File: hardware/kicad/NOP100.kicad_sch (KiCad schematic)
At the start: 44 parts, among them CON1 MIKROBUS_MODULE_CONN, CON2 MIKROBUS_MODULE_CONN, J1 CAN, Q1 BSS138, Q2 BSS138, SW1 BUS, SW2 SW_Push, U1 NCS1S1205SC, U2 MCP2551-I-P, U3 Teensy_4.0, U4 74HC165, U6 NCS1S1203SC

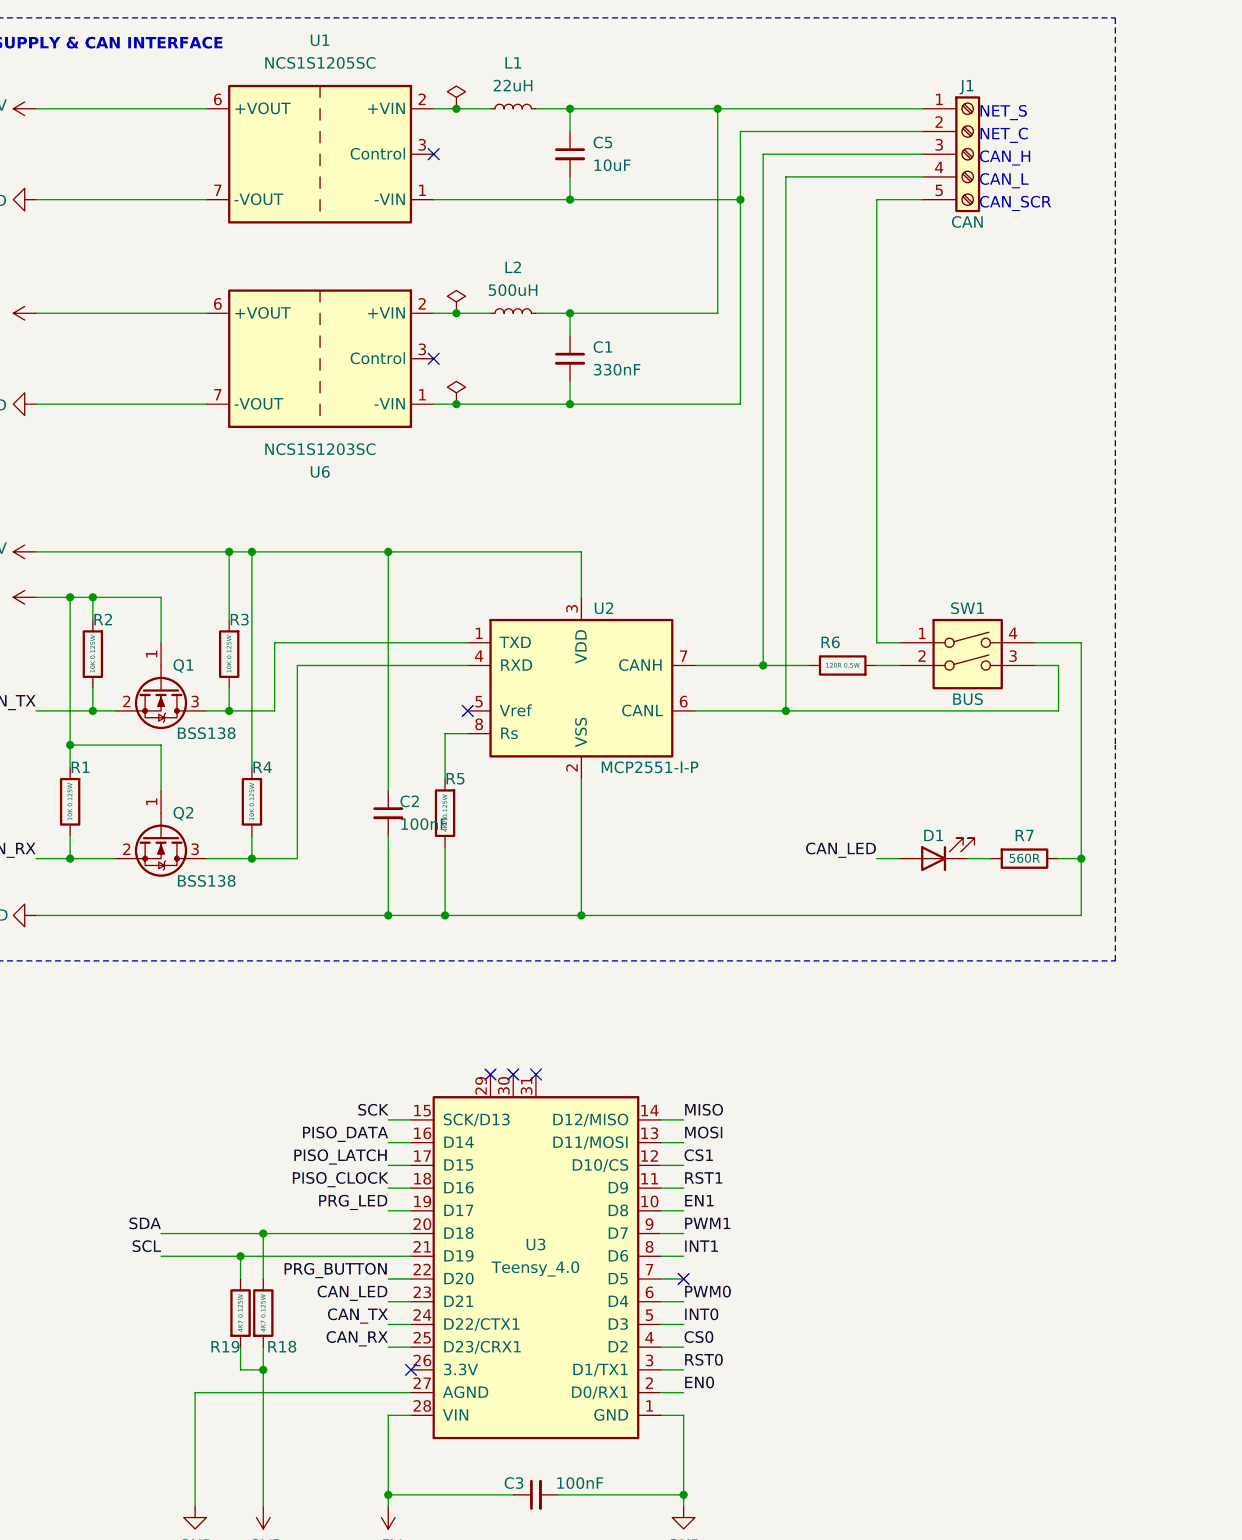
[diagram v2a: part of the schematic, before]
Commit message: Add 3.3VDC alternatives.
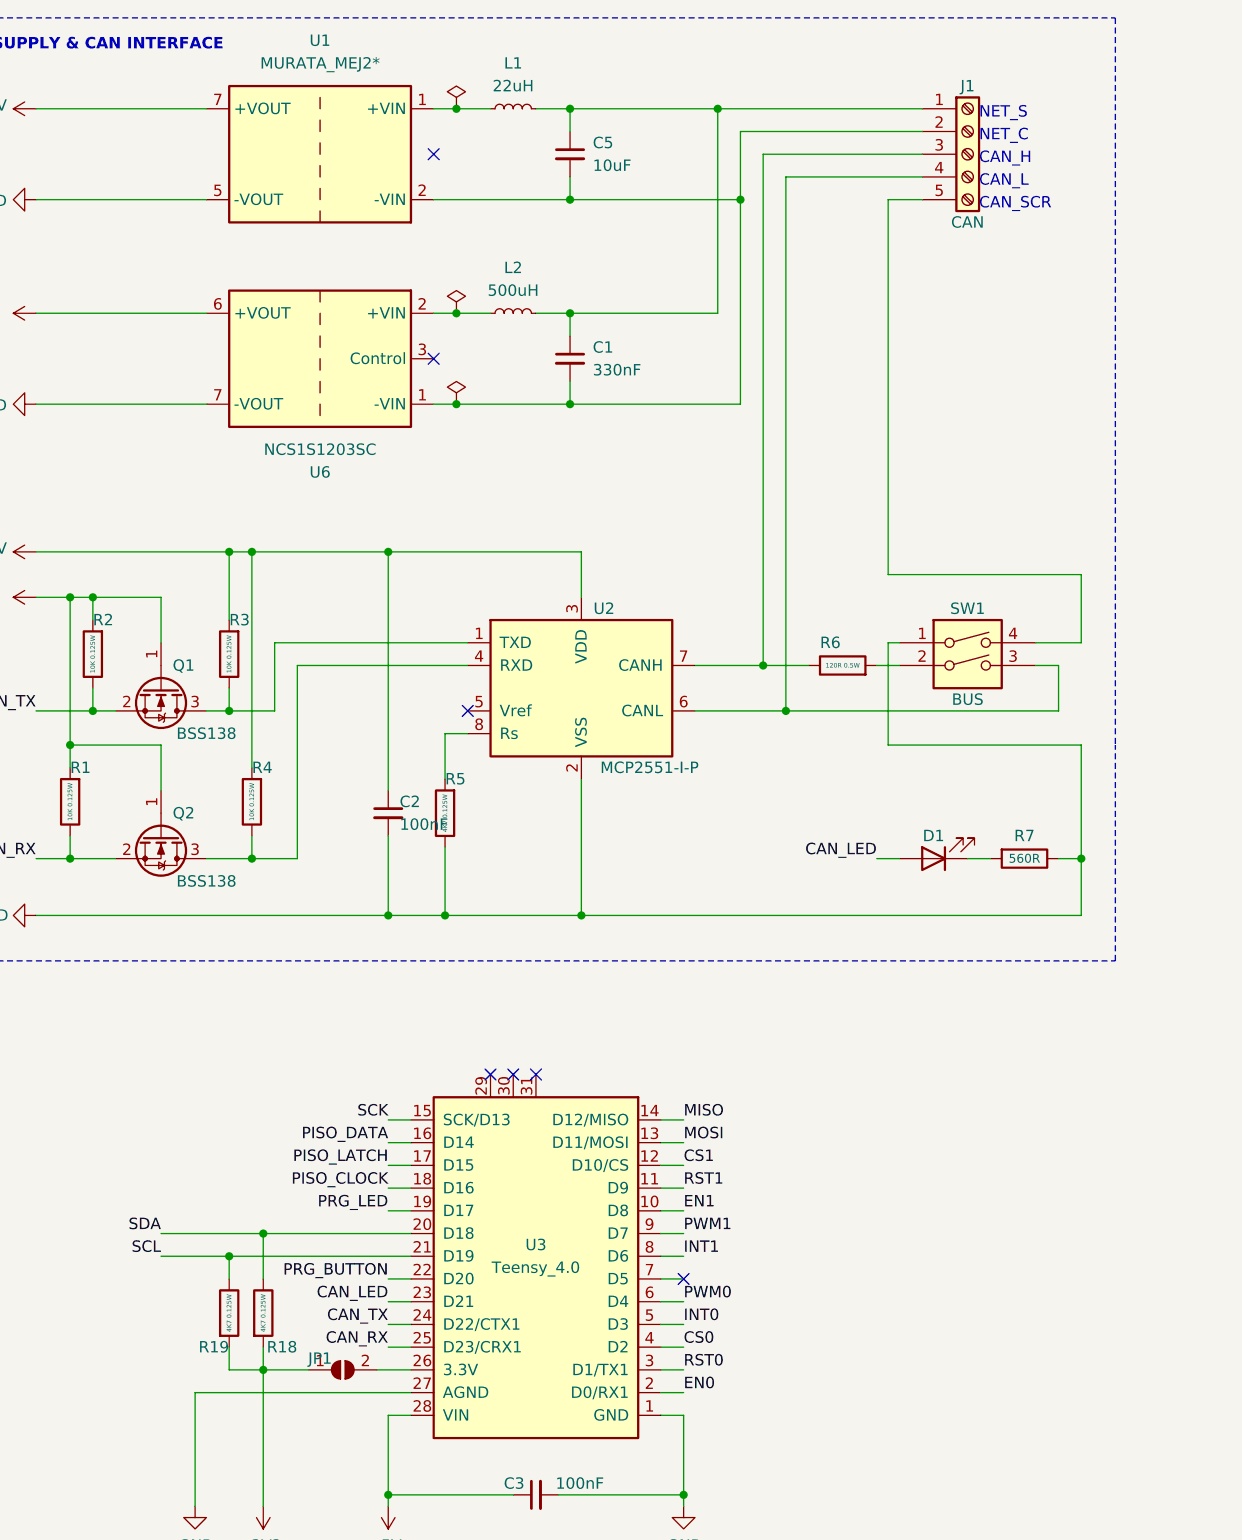
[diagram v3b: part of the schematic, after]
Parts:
- removed U1: NCS1S1205SC, Converter_DCDC:Converter_DCDC_Murata_NCS1SxxxxSC_THT, symbol Converter_DCDC:NCS1S1205SC
- added JP1: SolderJumper_2_Open, Jumper:SolderJumper-2_P1.3mm_Bridged_RoundedPad1.0x1.5mm, symbol Jumper:SolderJumper_2_Open
- added U1: MURATA_MEJ2*, pdjr:Murata-MEJ2*, symbol pdjr:MURATA_MEJ2*
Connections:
- net +3V3: now also JP1.1 (A)
- net +5V: now also U1.7 (+VOUT)
- net GND: now also SW1.1, U1.5 (-VOUT); no longer SW1.4
- net at J1.5 (Pin_5): now also SW1.4; no longer SW1.1
- net at C1.2, C5.2, J1.2 (Pin_2)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: now also U1.2 (-VIN)
- net at L1.1: now also U1.1 (+VIN)
- net at U3.26 (3.3V): now also JP1.2 (B)
- no-connect marks 15 -> 14
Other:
- moved on the sheet: R19
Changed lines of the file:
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@@
   (junction (at 199.39 71.12) (diameter 0) (color 0 0 0 0)
   )
+  (junction (at 144.78 107.95) (diameter 0) (color 0 0 0 0)
+  )
   (junction (at 53.34 165.1) (diameter 0) (color 0 0 0 0)
   )
@@
   (junction (at 240.03 41.91) (diameter 0) (color 0 0 0 0)
   )
-  (junction (at 144.78 107.95) (diameter 0) (color 0 0 0 0)
-  )
   (junction (at 237.49 39.37) (diameter 0) (color 0 0 0 0)
   )
@@
   (junction (at 88.9 114.3) (diameter 0) (color 0 0 0 0)
   )
-  (junction (at 50.8 152.4) (diameter 0) (color 0 0 0 0)
+  (junction (at 49.53 152.4) (diameter 0) (color 0 0 0 0)
   )
   (junction (at 194.31 71.12) (diameter 0) (color 0 0 0 0)
@@
   (junction (at 106.68 34.29) (diameter 0) (color 0 0 0 0)
   )
-  (no_connect (at 69.85 165.1))
   (no_connect (at 201.93 34.29))
   (no_connect (at 72.39 29.21))
@@
     (stroke (width 0) (type default))
   )
-  (wire (pts (xy 50.8 152.4) (xy 50.8 154.94))
+  (wire (pts (xy 49.53 152.4) (xy 49.53 154.94))
     (stroke (width 0) (type default))
   )
@@
     (stroke (width 0) (type default))
   )
-  (wire (pts (xy 50.8 165.1) (xy 50.8 162.56))
+  (wire (pts (xy 49.53 165.1) (xy 49.53 162.56))
     (stroke (width 0) (type default))
   )
@@
     (stroke (width 0) (type default))
   )
+  (wire (pts (xy 144.78 83.82) (xy 144.78 76.2))
+    (stroke (width 0) (type default))
+  )
   (wire (pts (xy 205.74 97.79) (xy 213.36 97.79))
     (stroke (width 0) (type default))
@@
     (stroke (width 0) (type default))
   )
-  (wire (pts (xy 121.92 34.29) (xy 121.92 83.82))
+  (wire (pts (xy 123.19 34.29) (xy 123.19 76.2))
     (stroke (width 0) (type default))
   )
@@
     (stroke (width 0) (type default))
   )
+  (wire (pts (xy 49.53 152.4) (xy 69.85 152.4))
+    (stroke (width 0) (type default))
+  )
   (wire (pts (xy 87.63 57.15) (xy 106.68 57.15))
     (stroke (width 0) (type default))
@@
     (stroke (width 0) (type default))
   )
-  (wire (pts (xy 144.78 83.82) (xy 144.78 107.95))
+  (wire (pts (xy 124.46 83.82) (xy 123.19 83.82))
     (stroke (width 0) (type default))
   )
@@
     (stroke (width 0) (type default))
   )
-  (wire (pts (xy 53.34 165.1) (xy 50.8 165.1))
-    (stroke (width 0) (type default))
-  )
-  (wire (pts (xy 121.92 34.29) (xy 127 34.29))
+  (wire (pts (xy 53.34 165.1) (xy 49.53 165.1))
+    (stroke (width 0) (type default))
+  )
+  (wire (pts (xy 123.19 34.29) (xy 127 34.29))
     (stroke (width 0) (type default))
   )
@@
     (stroke (width 0) (type dash))
   )
+  (wire (pts (xy 144.78 95.25) (xy 144.78 107.95))
+    (stroke (width 0) (type default))
+  )
   (wire (pts (xy 227.33 59.69) (xy 224.79 59.69))
     (stroke (width 0) (type default))
@@
     (stroke (width 0) (type default))
   )
+  (wire (pts (xy 123.19 95.25) (xy 144.78 95.25))
+    (stroke (width 0) (type default))
+  )
   (wire (pts (xy 67.31 139.7) (xy 69.85 139.7))
     (stroke (width 0) (type default))
@@
   )
   (wire (pts (xy 72.39 24.13) (xy 74.93 24.13))
-    (stroke (width 0) (type default))
-  )
-  (wire (pts (xy 50.8 152.4) (xy 69.85 152.4))
     (stroke (width 0) (type default))
   )
@@
     (stroke (width 0) (type default))
   )
+  (wire (pts (xy 53.34 165.1) (xy 58.42 165.1))
+    (stroke (width 0) (type default))
+  )
   (wire (pts (xy 142.24 91.44) (xy 142.24 86.36))
     (stroke (width 0) (type default))
@@
   )
   (wire (pts (xy 104.14 24.13) (xy 127 24.13))
+    (stroke (width 0) (type default))
+  )
+  (wire (pts (xy 123.19 83.82) (xy 123.19 95.25))
     (stroke (width 0) (type default))
   )
@@
     (stroke (width 0) (type default))
   )
+  (wire (pts (xy 123.19 76.2) (xy 144.78 76.2))
+    (stroke (width 0) (type default))
+  )
   (wire (pts (xy 97.79 137.16) (xy 100.33 137.16))
     (stroke (width 0) (type default))
@@
     (stroke (width 0) (type default))
   )
-  (wire (pts (xy 121.92 83.82) (xy 124.46 83.82))
-    (stroke (width 0) (type default))
-  )
   (wire (pts (xy 73.66 106.68) (xy 73.66 114.3))
     (stroke (width 0) (type default))
@@
     (stroke (width 0) (type default))
   )
-  (wire (pts (xy 41.91 152.4) (xy 50.8 152.4))
+  (wire (pts (xy 41.91 152.4) (xy 49.53 152.4))
     (stroke (width 0) (type default))
   )
@@
   )
   (wire (pts (xy 109.22 86.36) (xy 114.3 86.36))
+    (stroke (width 0) (type default))
+  )
+  (wire (pts (xy 66.04 165.1) (xy 69.85 165.1))
     (stroke (width 0) (type default))
   )
@@
     )
   )
+  (symbol (lib_id "pdjr:MURATA_MEJ2*") (at 59.69 29.21 180) (unit 1)
+    (in_bom yes) (on_board yes) (dnp no) (fields_autoplaced)
+    (property "Reference" "U1" (at 59.69 16.51 0)
+      (effects (font (size 1.27 1.27)))
+    )
+    (property "Value" "MURATA_MEJ2*" (at 59.69 19.05 0)
+      (effects (font (size 1.27 1.27)))
+    )
+    (property "Footprint" "pdjr:Murata-MEJ2*" (at 59.69 19.05 0)
+      (effects (font (size 1.27 1.27)) hide)
+    )
+    (property "Datasheet" "https://power.murata.com/data/power/ncl/kdc_ncs1.pdf" (at 60.325 29.21 0)
+      (effects (font (size 1.27 1.27)) hide)
+    )
+    (pin "2")
+    (pin "7")
+    (pin "5")
+    (pin "1")
+    (instances
+      (project "NOP100"
+        (path "/2cdb9afa-f75f-4c95-9ee5-dd44c25e8877"
+          (reference "U1") (unit 1)
+        )
+      )
+    )
+  )
   (symbol (lib_id "power:PWR_FLAG") (at 74.93 57.15 0) (unit 1)
     (in_bom yes) (on_board yes) (dnp no) (fields_autoplaced)
@@
     )
   )
-  (symbol (lib_id "Device:R") (at 50.8 158.75 0) (unit 1)
-    (in_bom yes) (on_board yes) (dnp no)
-    (property "Reference" "R19" (at 50.8 162.56 0)
+  (symbol (lib_id "Device:R") (at 49.53 158.75 0) (unit 1)
+    (in_bom yes) (on_board yes) (dnp no)
+    (property "Reference" "R19" (at 49.53 162.56 0)
       (effects (font (size 1.27 1.27)) (justify right))
     )
-    (property "Value" "4K7 0.125W" (at 50.8 158.75 90)
+    (property "Value" "4K7 0.125W" (at 49.53 158.75 90)
       (effects (font (size 0.508 0.508)))
     )
-    (property "Footprint" "Resistor_SMD:R_0805_2012Metric" (at 49.022 158.75 90)
-      (effects (font (size 1.27 1.27)) hide)
-    )
-    (property "Datasheet" "~" (at 50.8 158.75 0)
+    (property "Footprint" "Resistor_SMD:R_0805_2012Metric" (at 47.752 158.75 90)
+      (effects (font (size 1.27 1.27)) hide)
+    )
+    (property "Datasheet" "~" (at 49.53 158.75 0)
       (effects (font (size 1.27 1.27)) hide)
     )
@@
     )
   )
+  (symbol (lib_id "Jumper:SolderJumper_2_Open") (at 62.23 165.1 0) (unit 1)
+    (in_bom yes) (on_board yes) (dnp no)
+    (property "Reference" "JP1" (at 59.69 163.83 0)
+      (effects (font (size 1.27 1.27)))
+    )
+    (property "Value" "SolderJumper_2_Open" (at 62.23 161.29 0)
+      (effects (font (size 1.27 1.27)) hide)
+    )
+    (property "Footprint" "Jumper:SolderJumper-2_P1.3mm_Bridged_RoundedPad1.0x1.5mm" (at 62.23 165.1 0)
+      (effects (font (size 1.27 1.27)) hide)
+    )
+    (property "Datasheet" "~" (at 62.23 165.1 0)
+      (effects (font (size 1.27 1.27)) hide)
+    )
+    (pin "2")
+    (pin "1")
+    (instances
+      (project "NOP100"
+        (path "/2cdb9afa-f75f-4c95-9ee5-dd44c25e8877"
+          (reference "JP1") (unit 1)
+        )
+      )
+    )
+  )
   (symbol (lib_id "Device:C_Small") (at 87.63 29.21 0) (unit 1)
     (in_bom yes) (on_board yes) (dnp no) (fields_autoplaced)
@@
         )
       )
-    )
-  )
-  (symbol (lib_id "Converter_DCDC:NCS1S1205SC") (at 59.69 29.21 0) (mirror y) (unit 1)
-    (in_bom yes) (on_board yes) (dnp no)
-    (property "Reference" "U1" (at 59.69 16.51 0)
-      (effects (font (size 1.27 1.27)))
-    )
-    (property "Value" "NCS1S1205SC" (at 59.69 19.05 0)
-      (effects (font (size 1.27 1.27)))
-    )
-    (property "Footprint" "Converter_DCDC:Converter_DCDC_Murata_NCS1SxxxxSC_THT" (at 59.69 39.37 0)
-      (effects (font (size 1.27 1.27)) hide)
-    )
-    (property "Datasheet" "https://power.murata.com/data/power/ncl/kdc_ncs1.pdf" (at 60.325 29.21 0)
-      (effects (font (size 1.27 1.27)) hide)
-    )
-    (pin "2")
-    (pin "1")
-    (pin "3")
-    (pin "6")
-    (pin "7")
-    (instances
-      (project "NOP100"
-        (path "/2cdb9afa-f75f-4c95-9ee5-dd44c25e8877"
-          (reference "U1") (unit 1)
-        )
-      )

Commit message: Create Gerbers
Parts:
- CON1: value MIKROBUS_MODULE_CONN -> CLICK MODULE 0
- CON2: value MIKROBUS_MODULE_CONN -> CLICK MODULE 1
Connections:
- no-connect marks 14 -> 13
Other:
- note added: "Optional 3.3VDC supply"
- title: NOP100 Generic N2K Module -> NOP100 N2K Module with MikroBus
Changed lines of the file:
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@@
   (paper "A4")
   (title_block
-    (title "NOP100 Generic N2K Module")
-    (date "2022-06-11")
+    (title "NOP100 N2K Module with MikroBus")
+    (date "2024-07-15")
     (rev "2.0.0")
     (company "PDJR <preeve@pdjr.eu>")
@@
   )
   (no_connect (at 201.93 34.29))
-  (no_connect (at 72.39 29.21))
   (no_connect (at 213.36 110.49))
   (no_connect (at 213.36 137.16))
@@
     (stroke (width 0) (type default))
   )
-  (polyline (pts (xy -7.62 97.79) (xy -142.24 97.79))
-    (stroke (width 0) (type dash))
-  )
   (wire (pts (xy 45.72 167.64) (xy 45.72 180.34))
     (stroke (width 0) (type default))
@@
     (stroke (width 0) (type default))
   )
+  (polyline (pts (xy 17.78 40.64) (xy 97.79 40.64))
+    (stroke (width 0) (type dot))
+  )
   (wire (pts (xy 57.15 86.36) (xy 57.15 107.95))
     (stroke (width 0) (type default))
@@
     (stroke (width 0) (type default))
   )
+  (polyline (pts (xy 97.79 40.64) (xy 97.79 68.58))
+    (stroke (width 0) (type dot))
+  )
   (wire (pts (xy 72.39 24.13) (xy 74.93 24.13))
     (stroke (width 0) (type default))
@@
     (stroke (width 0) (type default))
   )
+  (polyline (pts (xy 97.79 68.58) (xy 17.78 68.58))
+    (stroke (width 0) (type dot))
+  )
   (wire (pts (xy 53.34 149.86) (xy 53.34 154.94))
     (stroke (width 0) (type default))
@@
     (stroke (width 0) (type default))
   )
+  (polyline (pts (xy 17.78 40.64) (xy 17.78 68.58))
+    (stroke (width 0) (type dot))
+  )
   (wire (pts (xy 100.33 170.18) (xy 97.79 170.18))
     (stroke (width 0) (type default))
@@
   (text "NET_S" (at 133.35 25.4 0)
     (effects (font (size 1.27 1.27)) (justify left bottom))
+  )
+  (text "Optional 3.3VDC supply" (at 19.05 67.31 0)
+    (effects (font (size 1.27 1.27) italic) (justify left bottom))
   )
   (label "PWM1" (at 213.36 142.24 180) (fields_autoplaced)
@@
       (effects (font (size 1.27 1.27)))
     )
-    (property "Value" "MIKROBUS_MODULE_CONN" (at 223.52 120.65 0)
+    (property "Value" "CLICK MODULE 1" (at 223.52 120.65 0)
       (effects (font (size 1.27 1.27)))
     )
@@
       (effects (font (size 1.27 1.27)))
     )
-    (property "Value" "MIKROBUS_MODULE_CONN" (at 223.52 93.98 0)
-      (effects (font (size 1.27 1.27)))
-    )
+    (property "Value" "CLICK MODULE 0" (at 223.52 93.98 0)
+      (effects (font (size 1.27 1.27)))
+    )

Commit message: Lots of tweaks
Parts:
- R6: footprint Resistor_THT:R_Axial_DIN0207_L6.3mm_D2.5mm_P7.62mm_Horizontal -> Resistor_SMD:R_1206_3216Metric
- SW2: footprint Button_Switch_SMD:SW_Push_1P1T_NO_Vertical_Wuerth_434133025816 -> Button_Switch_SMD:SW_SPST_PTS810
- U4: footprint Package_SO:SO-16_3.9x9.9mm_P1.27mm -> Package_SO:SOIC-16_3.9x9.9mm_P1.27mm
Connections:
- net CS0: now also U3.8 (D6); no longer U3.4 (D2)
- net EN0: now also U3.6 (D4); no longer U3.2 (D0/RX1)
- net INT0: now also U3.4 (D2); no longer U3.5 (D3)
- net INT1: now also U3.9 (D7); no longer U3.8 (D6)
- net PWM0: now also U3.5 (D3); no longer U3.6 (D4)
- net PWM1: now also U3.11 (D9); no longer U3.9 (D7)
- net RX: now reaches CON2.P13 (RX)
- net RX: now also CON1.P13 (RX), U3.2 (D0/RX1)
- net TX: now reaches CON2.P14 (TX)
- net TX: now also CON1.P14 (TX), U3.3 (D1/TX1)
- net RST: now reaches U3.7 (D5)
- net RST: now also CON1.P2 (RST), CON2.P2 (RST)
- removed net RST0: CON1.P2 (RST), U3.3 (D1/TX1)
- removed net RST1: CON2.P2 (RST), U3.11 (D9)
- no-connect marks 13 -> 8
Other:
- moved on the sheet: R20, R21
